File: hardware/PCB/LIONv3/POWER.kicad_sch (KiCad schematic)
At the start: 23 parts, among them U1 TPS259474ARPWR, U3 XL-1608UGC-04, U4 TLV75533PDQNR, U8 XL-1608SURC-06, U9 INA226AIDGSR

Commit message: feat(hardware): finish ESP32-C6 electrical schematic
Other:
- title: (none) -> LIONv3
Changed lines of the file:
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@@
 	(generator_version "10.0")
 	(paper "A4")
+	(title_block
+		(title "LIONv3")
+		(date "2026-08-12")
+		(rev "0.1")
+		(comment 1 "v3-Rodrigo")
+		(comment 2 "Rodrigo")
+		(comment 3 "2026-08-12")
+	)
 	(text "POWER CURRENT MONITOR"
 		(exclude_from_sim no)
@@
 		)
 	)
-	(text_box "PC/104 HEADERS"
+	(text_box "POWER CURRENT MONITOR"
 		(exclude_from_sim no)
 		(at 13.97 71.12 0)
@@
 		)
 	)
-	(text_box "LDO 3.3V"
+	(text_box "LEDS"
 		(exclude_from_sim no)
 		(at 213.36 13.97 0)

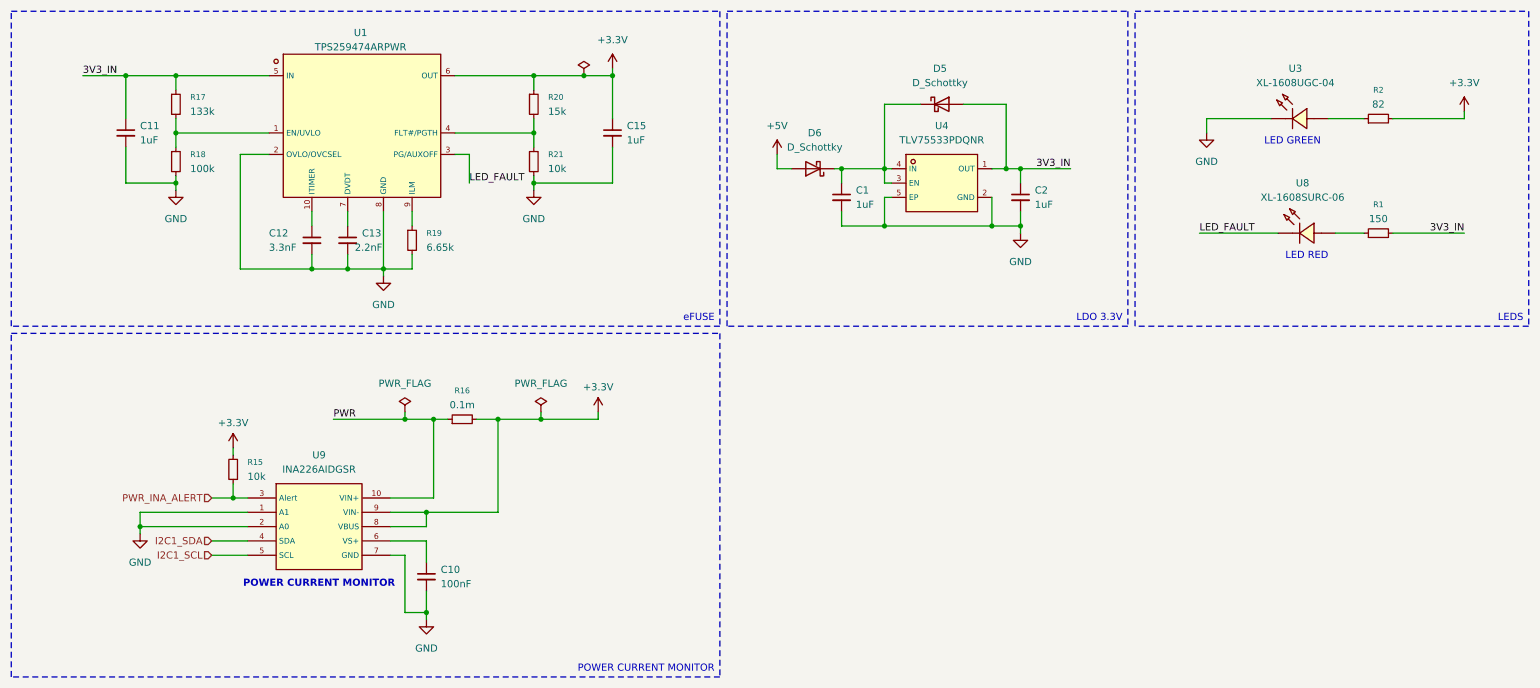
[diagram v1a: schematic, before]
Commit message: feat(hardware): add MOLEX connectors
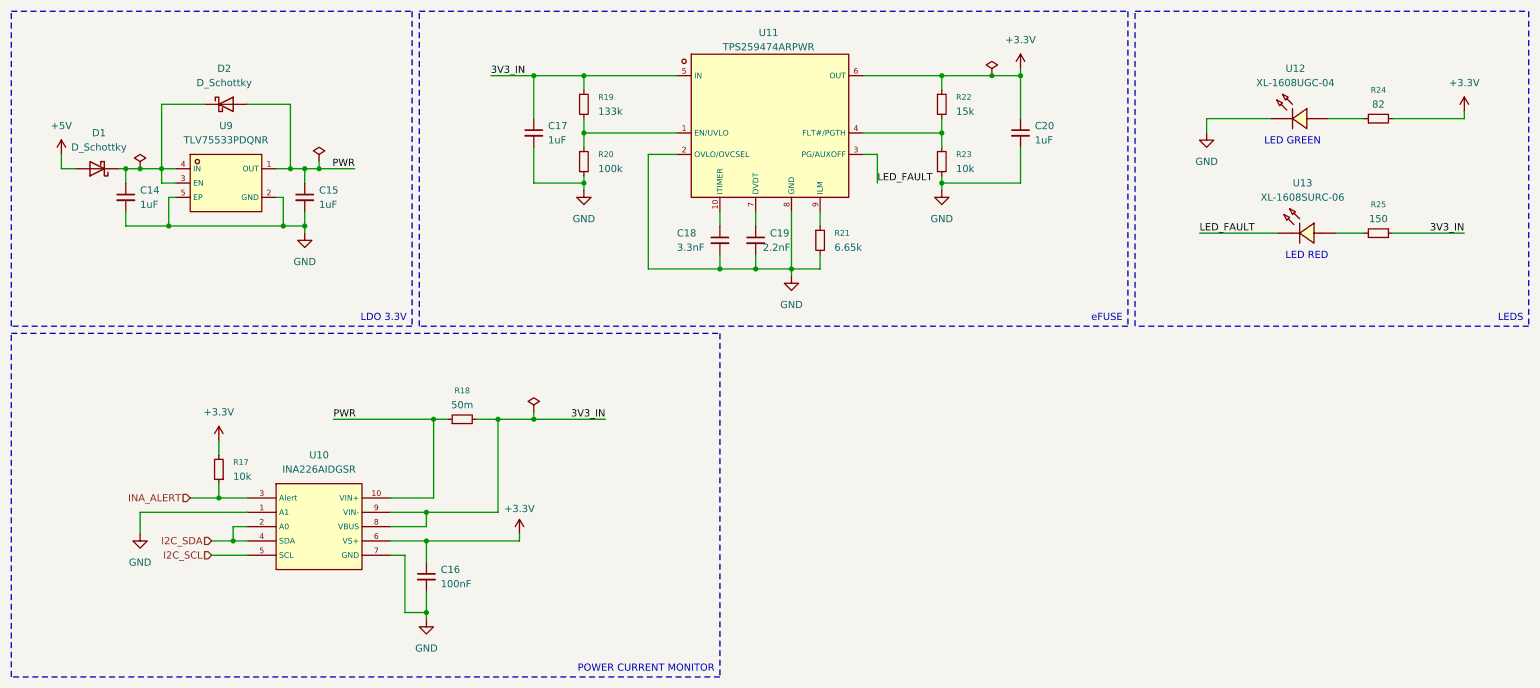
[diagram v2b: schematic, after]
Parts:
- removed R15: 10k, Resistor_SMD:R_0402_1005Metric, symbol Device:R_Small
- added R17: 10k, Resistor_SMD:R_0402_1005Metric, symbol Device:R_Small
- C14: renamed from C1; LCSC (none) -> C15849
- C15: renamed from C2; LCSC (none) -> C15849
- C16: renamed from C10; LCSC (none) -> C307331
- C17: renamed from C11; LCSC (none) -> C15849
- C18: renamed from C12; LCSC (none) -> C3881585
- C19: renamed from C13; LCSC (none) -> C2987940
- C20: renamed from C15; LCSC (none) -> C15849
- D1: renamed from D6; footprint Diode_SMD:D_0402_1005Metric -> LIONv3-Footprints:X2-DFN1006-2_L1.0-W0.6-P0.65-RD; LCSC (none) -> C2837790
- D2: renamed from D5; footprint Diode_SMD:D_0402_1005Metric -> LIONv3-Footprints:X2-DFN1006-2_L1.0-W0.6-P0.65-RD; LCSC (none) -> C2837790
- R18: renamed from R16; value 0.1m -> 50m; footprint TET-Footprints:RES-SMD_L6.3-W3.1-1 -> LIONv3-Footprints:R1206; LCSC C695817 -> C20608719
- R19: renamed from R17; LCSC (none) -> C25753
- R20: renamed from R18; LCSC (none) -> C25741
- R21: renamed from R19; LCSC (none) -> C853381
- R22: renamed from R20; LCSC (none) -> C25756
- R23: renamed from R21; LCSC (none) -> C25744
- R24: renamed from R2; LCSC (none) -> C2909389
- R25: renamed from R1; LCSC (none) -> C2909321
- U10: renamed from U9; symbol TET-Symbols:INA226AIDGSR -> LIONv3-Symbols:INA226AIDGSR
- renumbered U1 to U11, U3 to U12, U8 to U13, U4 to U9
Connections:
- net +3.3V: now also C16.1, U10.6 (VS+), R17.2; no longer R18.2, U10.8 (VBUS), U10.9 (VIN-)
- net 3V3_IN: now also R18.2, U10.8 (VBUS), U10.9 (VIN-); no longer C15.1, D2.2 (A), U9.1 (OUT)
- net GND: no longer U10.2 (A0)
- net PWR: now also C15.1, D2.2 (A), U9.1 (OUT)
- net I2C1_SCL renamed I2C_SCL
- net I2C1_SDA renamed I2C_SDA
- net I2C_SDA: now also U10.2 (A0)
- net PWR_INA_ALERT renamed INA_ALERT
- net INA_ALERT: now also R17.1
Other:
- note removed: "POWER CURRENT MONITOR"
- moved on the sheet: C14, C15, C17, C18, C19, C20, D1, D2, R19, R20, R21, R22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

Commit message: feat(hardware): finish board schematic
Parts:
- removed C14, C15: 1uF, Capacitor_SMD:C_0603_1608Metric, symbol Device:C_Small
- removed D1, D2: D_Schottky, LIONv3-Footprints:X2-DFN1006-2_L1.0-W0.6-P0.65-RD, symbol Device:D_Schottky
- removed U9: TLV75533PDQNR, LIONv3-Footprints:X2SON-4_L1.0-W1.0-P0.65-TL-EP, symbol LIONv3-Symbols:TLV75533PDQNR
- added C21, C22: 2.2uF, Capacitor_SMD:C_0603_1608Metric, symbol Device:C_Small
- added D3, D4: D_Schottky, LIONv3-Footprints:X2-DFN1006-2_L1.0-W0.6-P0.65-RD, symbol Device:D_Schottky
- added R30: 20k, Resistor_SMD:R_0402_1005Metric, symbol Device:R_Small
- added R31: 10k, Resistor_SMD:R_0402_1005Metric, symbol Device:R_Small
- added U20: TLV76733DRVR, LIONv3-Footprints:WSON-6_L2.0-W2.0-P0.65-TL-EP, symbol LIONv3-Symbols:TLV76733DRVR
- R21: value 6.65k -> 3.32k; LCSC C853381 -> C2998161
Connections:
- net +3.3V: no longer C16.1, R17.2, U10.6 (VS+)
- net +5V: now also D3.2 (A)
- net 3V3_IN: now also R30.1
- net GND: now also C21.2, C22.2, R31.2, U20.3 (GND), U20.5 (GND), U20.7 (EP); no longer U11.2 (OVLO/OVCSEL)
- net PWR: now also C16.1, R17.2, U10.6 (VS+), C22.1, D4.2 (A), U20.1 (OUT), U20.2 (FB/SNS)
- new net: C21.1, D3.1 (K), D4.1 (K), U20.4 (EN), U20.6 (IN)
- new net: R30.2, R31.1, U11.2 (OVLO/OVCSEL)
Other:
- note added: "2.8V - 3.6V Max 1A"
- note added: "3.3V@800mA"
- note added: "VALIDATED"
- moved on the sheet: C17, C18, C19, C20, R19, R20, R21, R22, R23, U11

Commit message: feat(hardware): add TPS259474ARPWR PCB circuit
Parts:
- removed R30: 20k, Resistor_SMD:R_0402_1005Metric, symbol Device:R_Small
- removed R31: 10k, Resistor_SMD:R_0402_1005Metric, symbol Device:R_Small
- added R32: 34.8k, Resistor_SMD:R_0402_1005Metric, symbol Device:R_Small
- R19: value 133k -> 60.4k; LCSC C25753 -> C2998058
- R20: value 100k -> 10k; LCSC C25741 -> C25744
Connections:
- net GND: now also R32.2; no longer R20.2
- net 5V_D: now reaches C21.1, D3.1 (K), D4.1 (K), U20.4 (EN), U20.6 (IN)
- net at U11.2 (OVLO/OVCSEL): now also R20.2, R32.1
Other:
- moved on the sheet: C17
